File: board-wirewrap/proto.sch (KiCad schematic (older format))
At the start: 54 parts, among them CON101 Micro_SD_Card, P1 AB, P101 Data, P102 Power, P103 DIL8, P2 CD, SW101 RESET, U1 DS8641-LR, U101 Am2908, U102 Am2908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

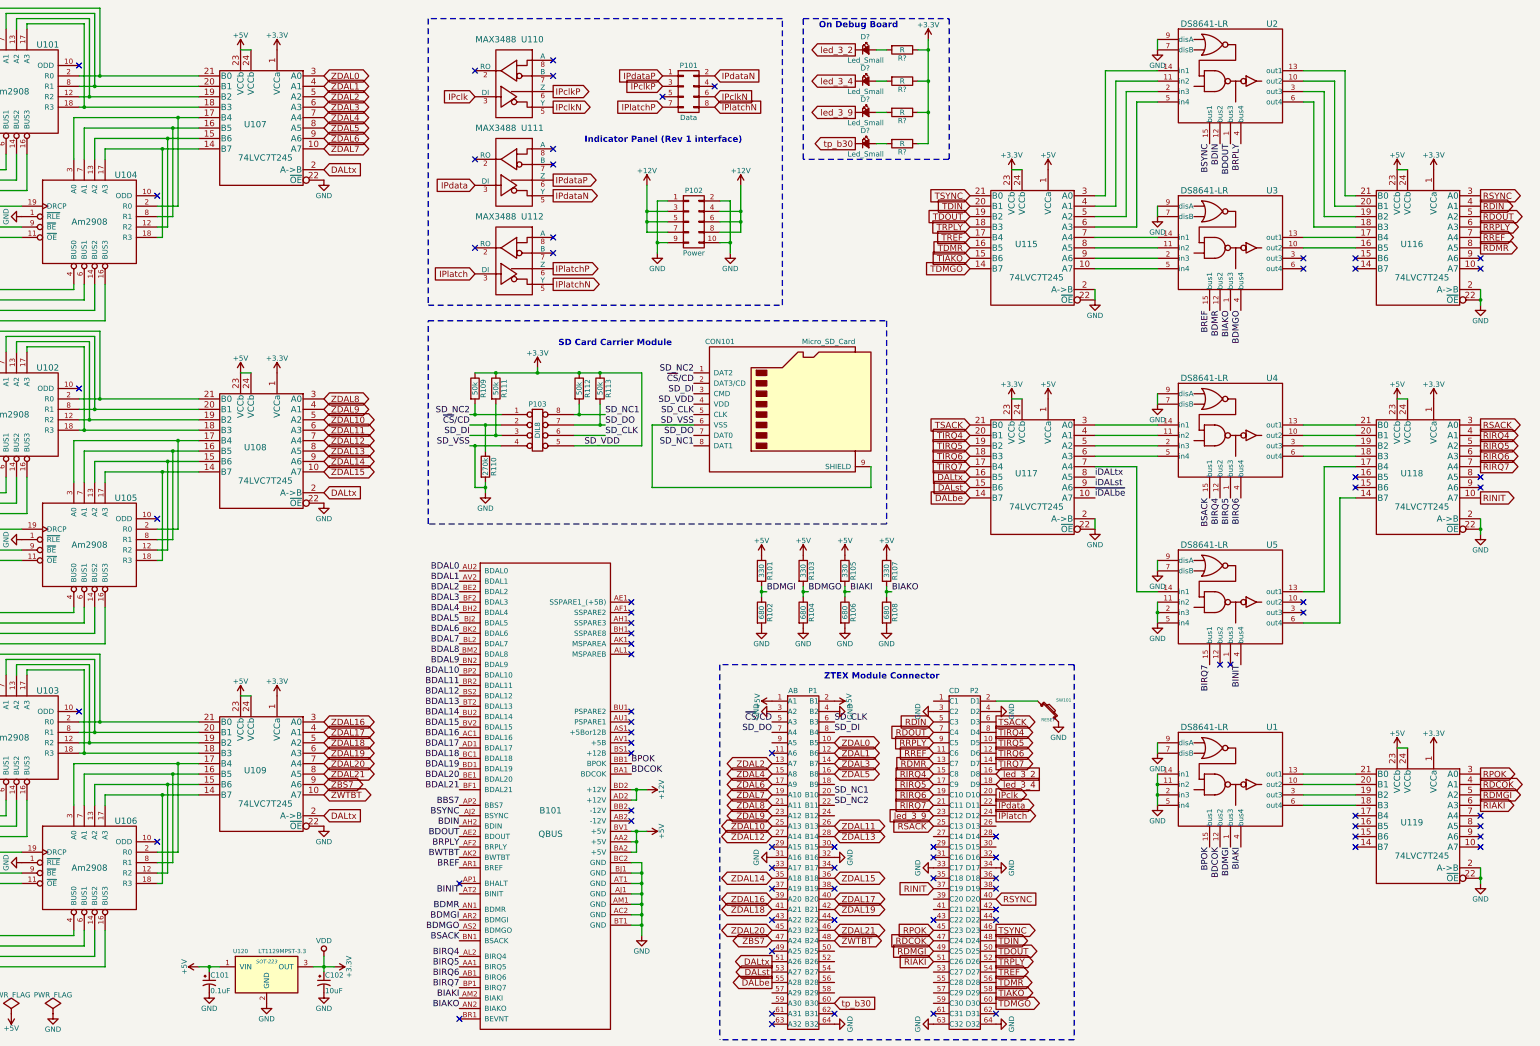
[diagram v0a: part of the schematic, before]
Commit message: Moved some wires around.
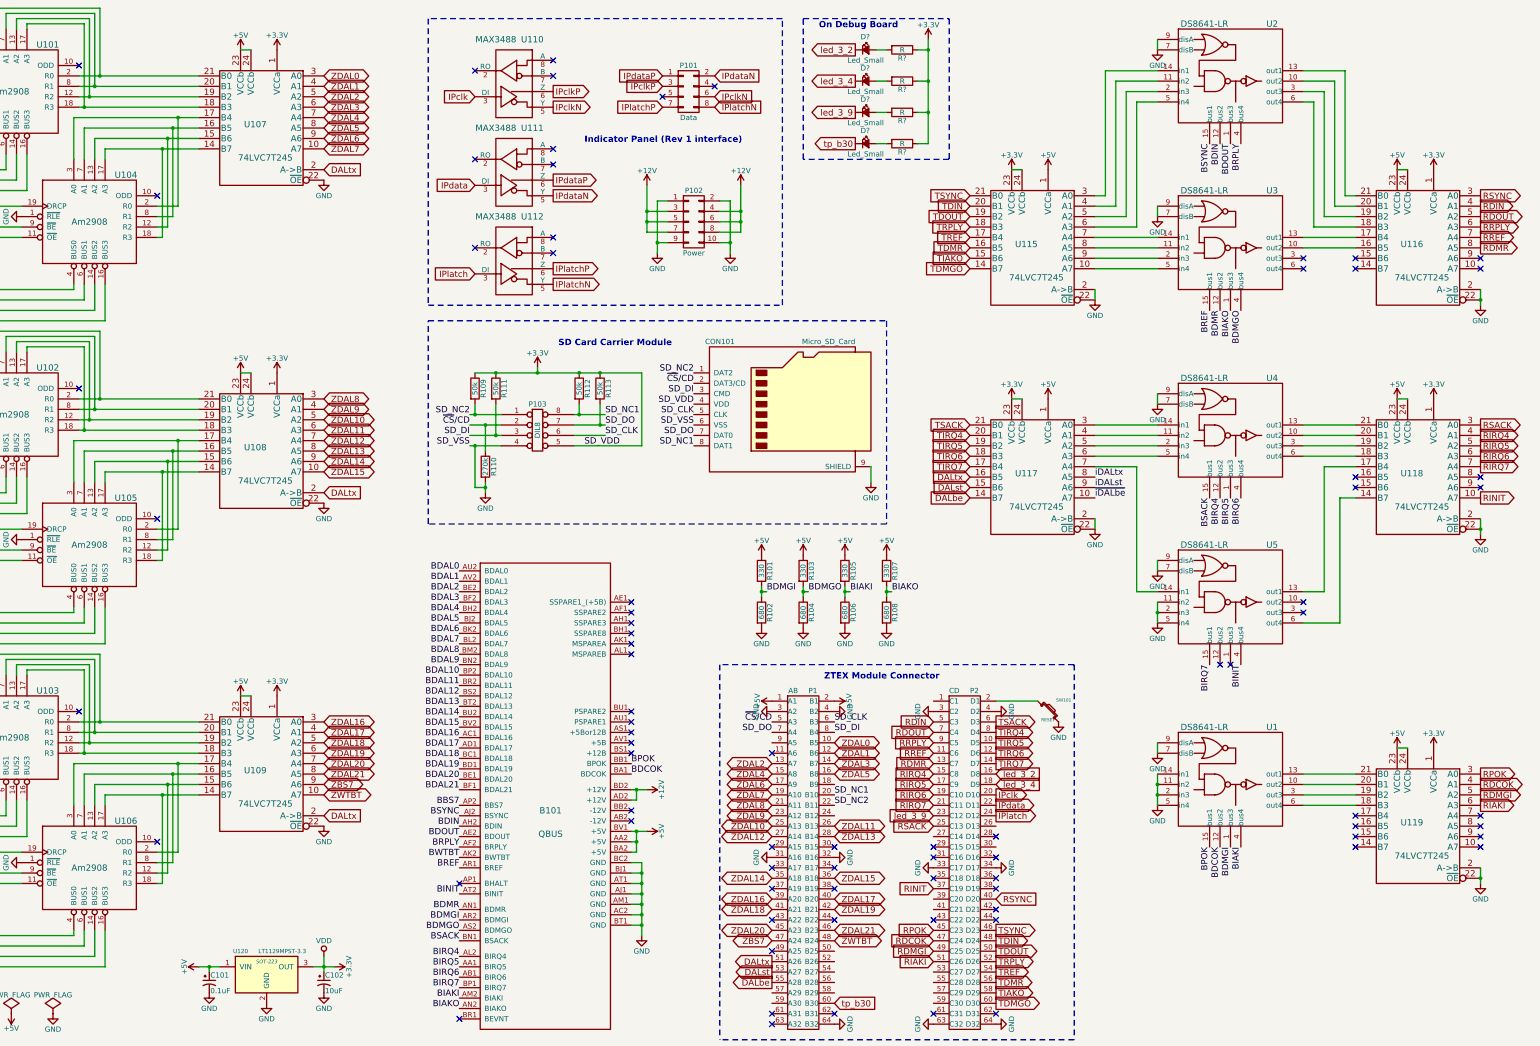
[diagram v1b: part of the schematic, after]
